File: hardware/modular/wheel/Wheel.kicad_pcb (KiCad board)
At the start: 4 copper layers, 55 x 60 mm, 87 parts, among them J11 WHEEL_POWER_2P, J5 GB1806 phase wires, J9 WHEEL_SIGNAL_30P, Q4 2N7002, Q5 AO3400A, U21 DRV8316RRGFR, U22 SN74LVC08APWR, U23 ADS7038IRTER, U24 SN74LVC125APWR, U26 SN74LVC125APWR, U30 TLV1811DBVR, U31 LM4040AIM3-2.5/NOPB

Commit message: Finish wheel routing and place split main PCB
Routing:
- net WHEEL_RUN_REQ: track 0.00 -> 52.2 mm
- net WHEEL_RUN_EN: track 0.00 -> 52.0 mm, vias 0 -> 4
- net WHEEL_PWM_A: track 0.00 -> 48.3 mm, vias 0 -> 4
- net ACT_DRIVE_EN: track 0.00 -> 47.8 mm, vias 0 -> 4
- net DRV_FAULT_LOCAL_N: track 0.00 -> 44.4 mm, vias 0 -> 6
- net WHEEL_PWM_C: track 0.00 -> 41.6 mm, vias 0 -> 4
- net WHEEL_PWM_B: track 0.00 -> 39.9 mm, vias 0 -> 4
- net DRV_MISO_LOCAL: track 0.00 -> 39.1 mm, vias 0 -> 2
- net +3V3: track 0.00 -> 38.8 mm, vias 0 -> 3
- net CS_DRV8316: track 0.00 -> 32.3 mm, vias 0 -> 2
- net SPI_MOSI: track 0.00 -> 27.6 mm, vias 0 -> 4
- net ADC2_MISO_LOCAL: track 0.00 -> 25.2 mm, vias 0 -> 2
- net SPI_SCLK: track 0.00 -> 24.8 mm, vias 0 -> 2
- net DRV_INHC: track 0.00 -> 23.1 mm, vias 0 -> 2
- net ADC2_CS_LOCAL: track 0.00 -> 22.0 mm, vias 0 -> 2
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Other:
- board text added: "PROTO"
- board text added: "WHEEL 55 x 60 mm / ROUTED / MECHANICS AND QUALIFICATION PENDING"
- board text added: "Wheel 0.3"
- board text removed: "UNROUTED"
- board text removed: "WHEEL 55 x 60 mm / POWER + ANALOG ROUTED / DIGITAL PENDING"
- board text removed: "Wheel 0.2"

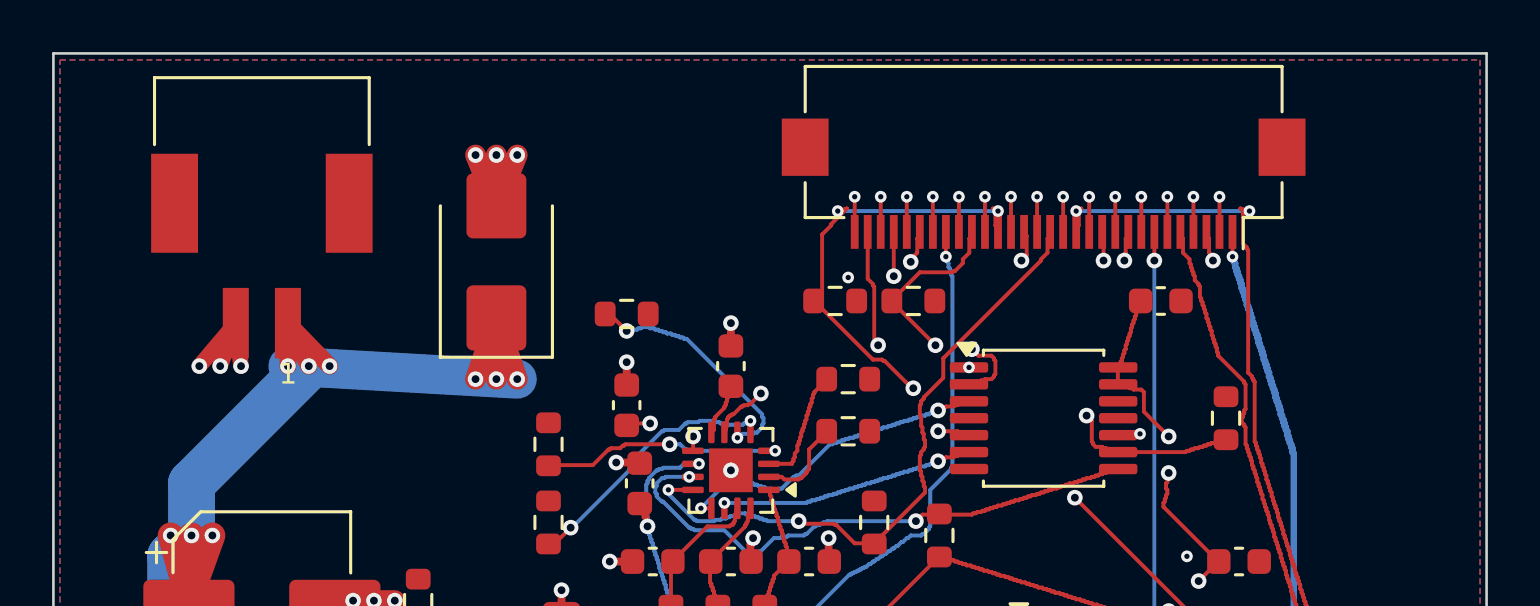
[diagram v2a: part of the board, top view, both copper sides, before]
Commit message: Prepare wired Rev-A bench boards and submit manufacturing review
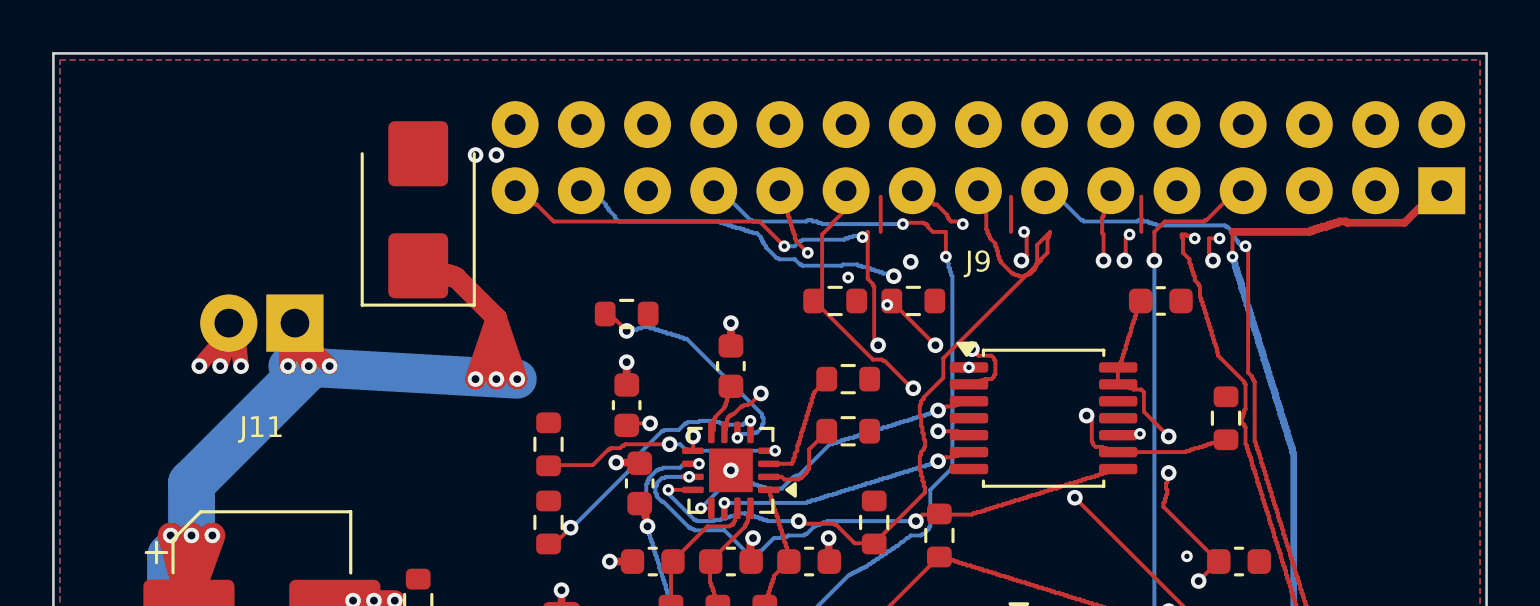
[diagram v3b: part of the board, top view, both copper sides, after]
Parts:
- J11: value WHEEL_POWER_2P -> Soldered wires Power_1x02; footprint MagMouseModular:JST_PA_SM02B-PASS_1x02_P2.00mm_Horizontal -> MagMouseModular:Wire_Power_1x02_P2.54mm
- J9: value WHEEL_SIGNAL_30P -> Soldered wires Signal_2x15; footprint Connector_FFC-FPC:Hirose_FH12-30S-0.5SH_1x30-1MP_P0.50mm_Horizontal -> MagMouseModular:Wire_Signal_2x15_P2.54mm
- moved D6 3.61 mm to (14.0, 6.00)
- moved J9 2.69 mm to (35.5, 4.00)
- moved J11 1.35 mm to (8.00, 10.3), turned to 180 degrees
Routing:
- net GND: track 73.3 -> 50.9 mm, vias 77 -> 61
- net SPI_SCLK: track 24.8 -> 39.5 mm, vias 2 -> 4
- net SPI_MOSI: track 27.6 -> 39.6 mm
- net CS_DRV8316: track 32.3 -> 42.5 mm
- net DRV_MISO_LOCAL: track 39.1 -> 48.8 mm, vias 2 -> 3
- net +3V3: track 38.8 -> 47.5 mm
- net WHEEL_RUN_REQ: track 52.2 -> 60.0 mm, vias 0 -> 1
- net MOTOR_SPI_MOSI: track 20.4 -> 13.0 mm, vias 4 -> 2
- net DRV_FAULT_LOCAL_N: track 44.4 -> 51.3 mm, vias 6 -> 7
- net ADC2_MISO_LOCAL: track 25.2 -> 31.6 mm
- net CS_ADC2: track 15.1 -> 20.2 mm, vias 2 -> 4
- net ACT_DRIVE_EN: track 47.8 -> 51.8 mm
- net ACT_5V: track 236.6 -> 240.4 mm
- net WHEEL_PWM_C: track 41.6 -> 44.3 mm, vias 4 -> 5
- net MOTOR_SPI_SCLK: track 11.4 -> 13.9 mm, vias 2 -> 4
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
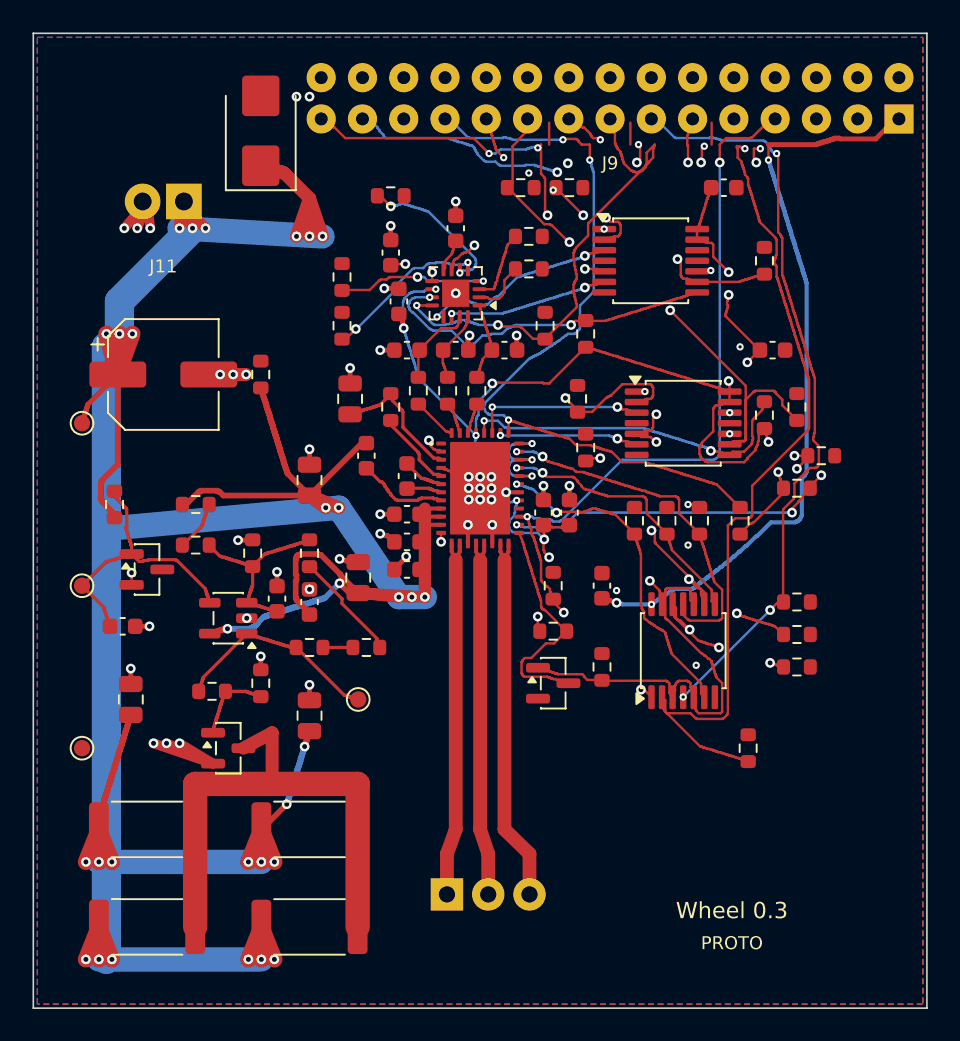
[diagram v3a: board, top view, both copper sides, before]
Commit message: Repair copper contacts and make manufacturing panel router-compatible
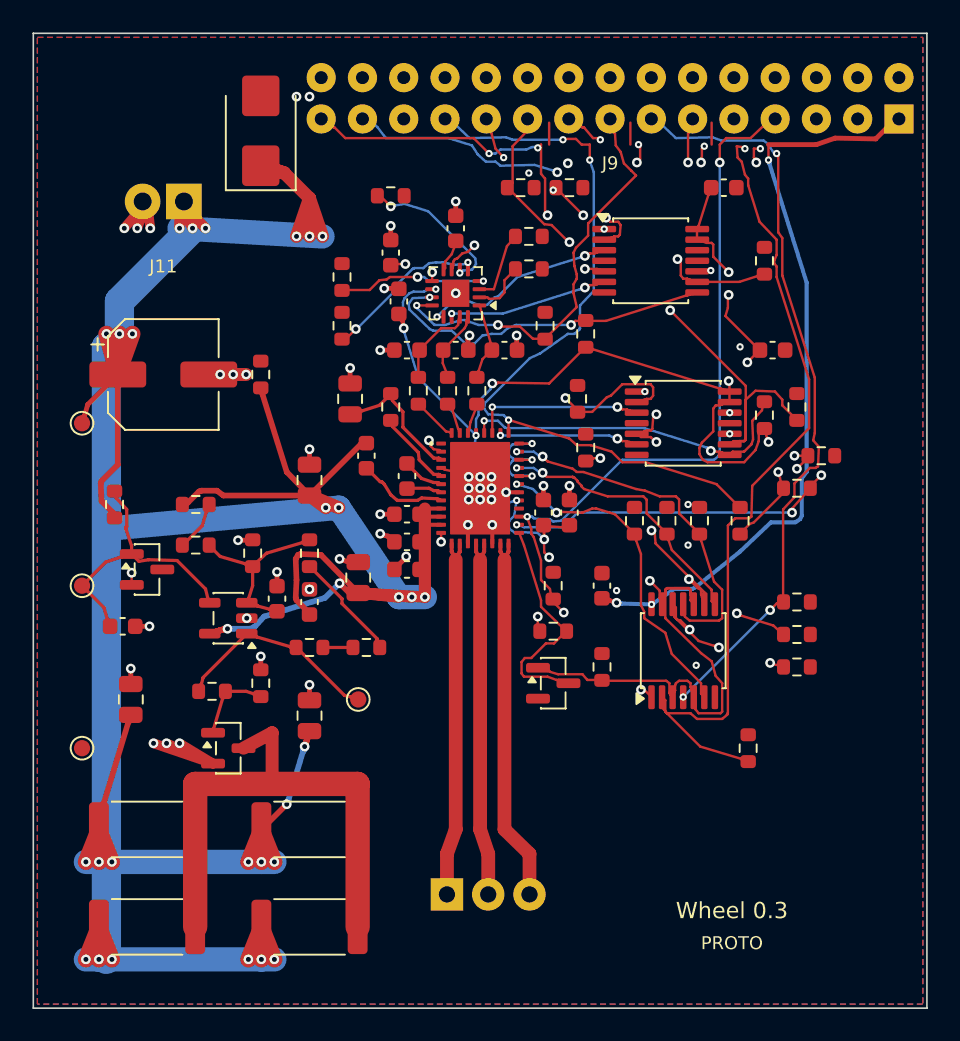
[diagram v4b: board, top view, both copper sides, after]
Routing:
- net ACT_5V: track 240.4 -> 248.3 mm
- net ADC2_MISO_LOCAL: track 31.6 -> 26.5 mm
- net DRV_AVDD: track 103.5 -> 101.7 mm
- net SPI_MOSI: track 39.6 -> 38.2 mm
- net DRV_MISO_LOCAL: track 48.8 -> 47.7 mm
- net WHEEL_RUN_REQ: track 60.0 -> 59.0 mm
- net DRV_INHC: track 23.1 -> 22.3 mm
- net DRV_FAULT_LOCAL_N: track 51.3 -> 50.6 mm
- net WHEEL_PWM_A: track 47.6 -> 46.8 mm
- net CS_DRV8316: track 42.5 -> 41.9 mm
- net ADC2_CS_LOCAL: track 22.0 -> 21.4 mm
- net DRV_INHA: track 21.0 -> 20.5 mm
